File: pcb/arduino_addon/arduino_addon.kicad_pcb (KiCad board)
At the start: 2 copper layers, 37 parts, among them P10 ADC2ADC, P11 ADC-DO, P12 ADC-DO, P13 ADC-DO, P14 ADC-DO, P15 DO, P2 Power, P3 Digital1, P4 Digital2, P5 BNC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

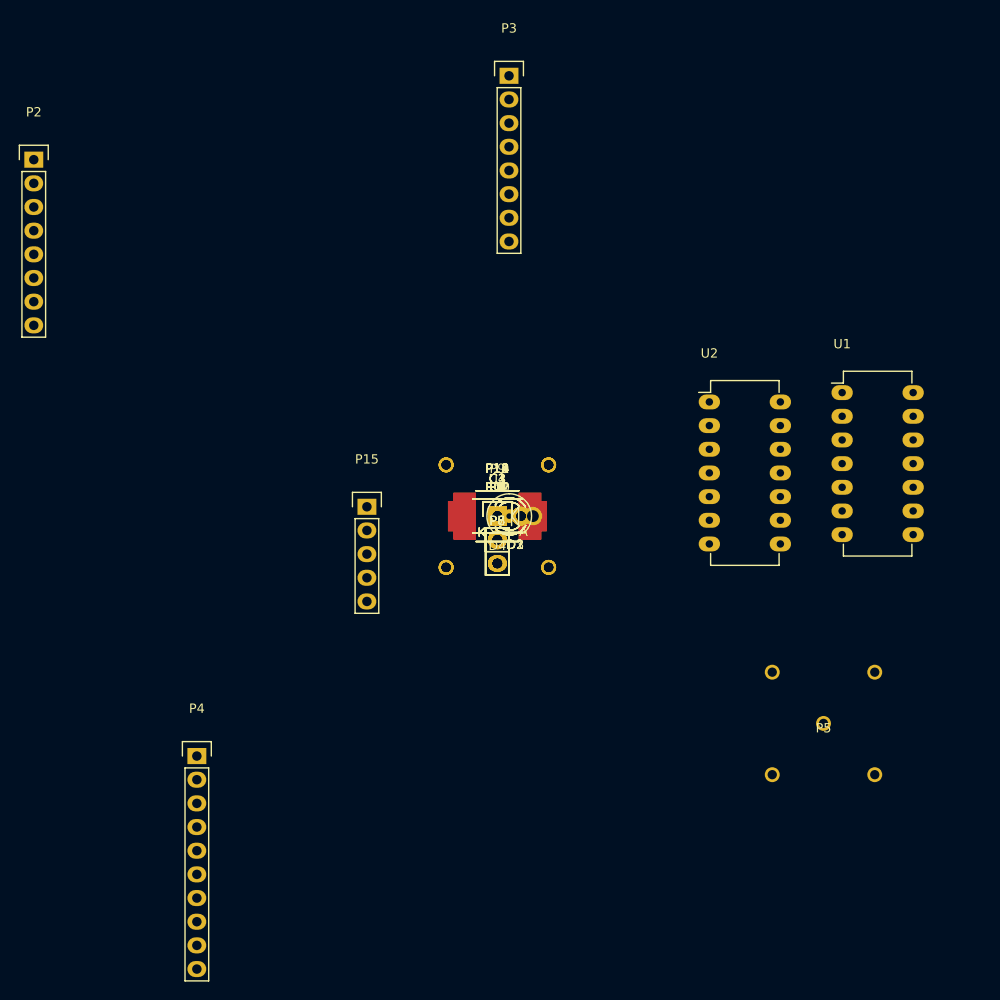
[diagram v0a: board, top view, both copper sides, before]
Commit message: pcb layout, no wiring
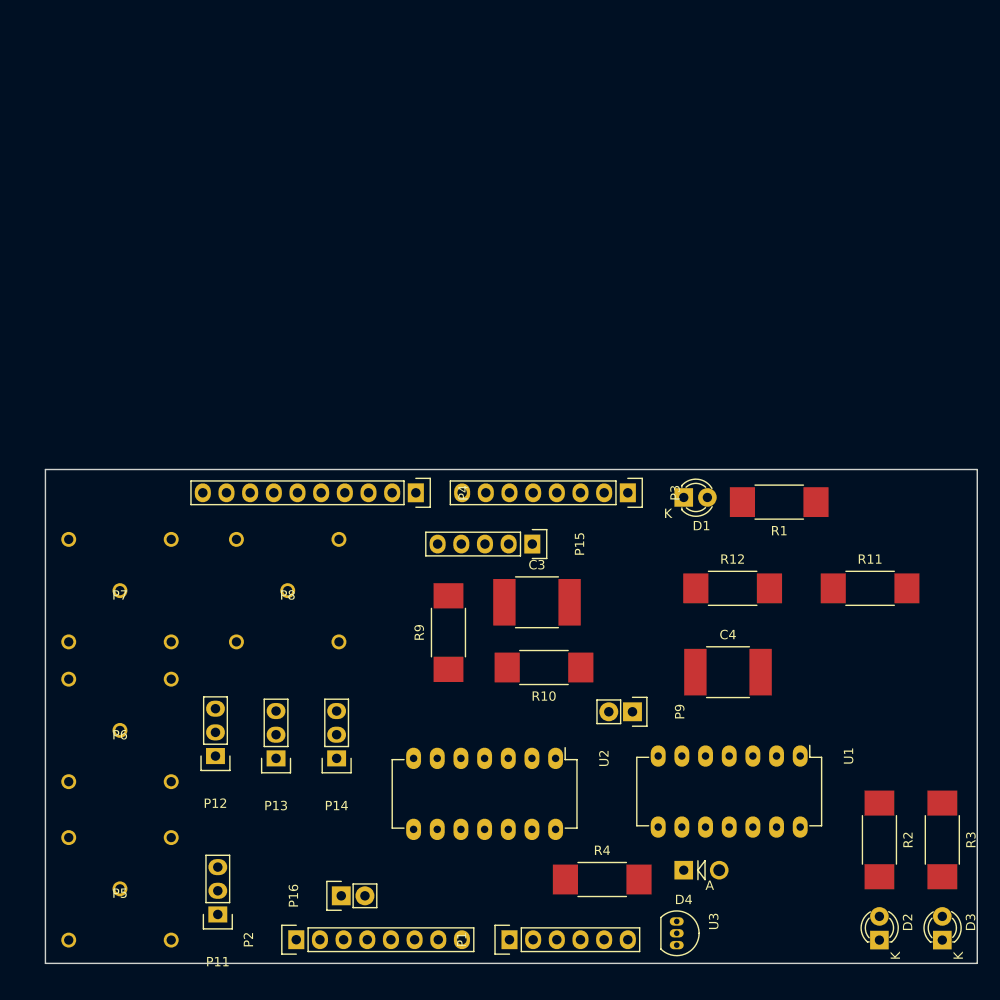
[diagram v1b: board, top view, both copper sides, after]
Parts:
- removed C1, C2: 12n, Capacitors_SMD:C_2220_HandSoldering
- removed P10: ADC2ADC, Pin_Headers:Pin_Header_Straight_1x02
- removed R5, R6: 100k, Resistors_SMD:R_2512_HandSoldering
- removed R7, R8: 10k, Resistors_SMD:R_2512_HandSoldering
- added P1: AnalogIn, Pin_Headers:Pin_Header_Straight_1x06, F.Cu at (149.8, 150.5)
- added P16: 3V3 ADC REF, Pin_Headers:Pin_Header_Straight_1x02, F.Cu at (131.8, 145.8)
- P9: value ADC2ADC -> DAC2ADC0
- moved P2 88.3 mm to (126.9, 150.5), turned to 90 degrees
- moved P5 77.6 mm to (108.0, 145.0)
- moved D3 66.0 mm to (196.2, 150.5), turned to 90 degrees
- moved D2 61.2 mm to (189.5, 150.5), turned to 90 degrees
- moved R3 59.1 mm to (196.2, 139.8), turned to 270 degrees
- moved R2 53.7 mm to (189.5, 139.8), turned to 270 degrees
- moved P11 52.2 mm to (118.5, 147.8), turned to 180 degrees
- moved U3 47.6 mm to (167.8, 148.5), turned to 270 degrees
- moved P6 46.6 mm to (108.0, 128.0)
- moved P3 46.5 mm to (162.5, 102.5), turned to 270 degrees
- moved D4 42.9 mm to (168.5, 143.0)
- moved U2 41.7 mm to (154.8, 131.0), turned to 270 degrees
- moved P7 41.3 mm to (108.0, 113.0)
- moved R11 40.7 mm to (188.5, 112.8)
- moved R4 40.6 mm to (159.8, 144.0)
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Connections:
- P4 pad 4: /D11 -> (no net)
- R4 pad 1: /AD5 -> /AD4
- U1 pad 1: /DAC1 -> (no net)
- U1 pad 2: Net-(R7-Pad1) -> (no net)
- U1 pad 3: Net-(R6-Pad1) -> (no net)
- U1 pad 8: /AD5 -> /AD4
- U3 pad 2: (no net) -> /AD5
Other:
- board outline added: 100 x 53 mm
- net class Default: clearance 0.2 -> 0.3; trace_width 0.25 -> 0.3; via_dia 0.6 -> 0.7; via_drill 0.4 -> 0.6
- rule trace_clearance: 0.2 -> 0.3

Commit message: arduino addon board pcb design is ready
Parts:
- moved R12 18.5 mm to (188.8, 123.5)
- moved D4 5.76 mm to (174.2, 143.2)
- moved R4 4.81 mm to (164.5, 143.2)
- moved R10 3.69 mm to (151.8, 124.5)
- moved C3 3.58 mm to (152.0, 117.8)
- moved R9 3.50 mm to (143.2, 121.0)
- moved P16 2.85 mm to (134.5, 145.0)
- turned C4 to 180 degrees
- turned R11 to 180 degrees
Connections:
- P16 pad 2: (no net) -> /AD0
- P2 pad 5: +5V -> (no net)
- P9 pad 2: (no net) -> /AI3
- U1 pad 4: +5V -> +3V3
- U2 pad 4: +5V -> +3V3
- U3 pad 1: +5V -> +3V3
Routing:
- net (no net): track 0.00 -> 611.8 mm
- net GND: track 0.00 -> 398.9 mm, vias 0 -> 5
- net +3V3: track 0.00 -> 127.2 mm, vias 0 -> 1
- net /D0: track 0.00 -> 96.5 mm, vias 0 -> 1
- net /D9: track 0.00 -> 91.1 mm, vias 0 -> 2
- net /D8: track 0.00 -> 82.6 mm, vias 0 -> 2
- net /D1: track 0.00 -> 74.4 mm, vias 0 -> 1
- net /D2: track 0.00 -> 54.2 mm, vias 0 -> 1
- net /AI3: track 0.00 -> 52.6 mm, vias 0 -> 1
- net /AI0: track 0.00 -> 45.3 mm, vias 0 -> 1
- net /D3: track 0.00 -> 45.1 mm, vias 0 -> 1
- net /AD0: track 0.00 -> 42.2 mm, vias 0 -> 1
- net /AD1: track 0.00 -> 41.8 mm
- net Net-(R11-Pad1): track 0.00 -> 41.4 mm, vias 0 -> 1
- net /DAC0: track 0.00 -> 36.9 mm, vias 0 -> 1
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- added copper zone on B.Cu, net GND
- added copper zone on F.Cu, net GND
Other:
- net class Default: trace_width 0.3 -> 0.6
- board text added: "RZ 2016"
